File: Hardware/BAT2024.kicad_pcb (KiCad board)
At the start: 2 copper layers, 0 parts

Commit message: Finalized schematic V1.0; minor changes to symbol library
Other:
- board outline added: 80 x 80 mm
- board text added: "Bachelorarbeit 2024 Stefano Nicora HSLU T&A | V1.0"
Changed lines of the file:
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@@
 	)
 	(net 0 "")
+	(gr_circle
+		(center 158.628 97.028)
+		(end 198.628 97.028)
+		(stroke
+			(width 0.2)
+			(type default)
+		)
+		(fill none)
+		(layer "Edge.Cuts")
+	)
+	(gr_text "Bachelorarbeit 2024\nStefano Nicora\nHSLU T&A | V1.0\n"
+		(at 148.336 130.556 0)
+		(layer "F.SilkS")
+		(effects
+			(font
+				(size 1.5 1.5)
+				(thickness 0.3)
+				(bold yes)
+			)
+			(justify left bottom)
+		)
+	)
 )

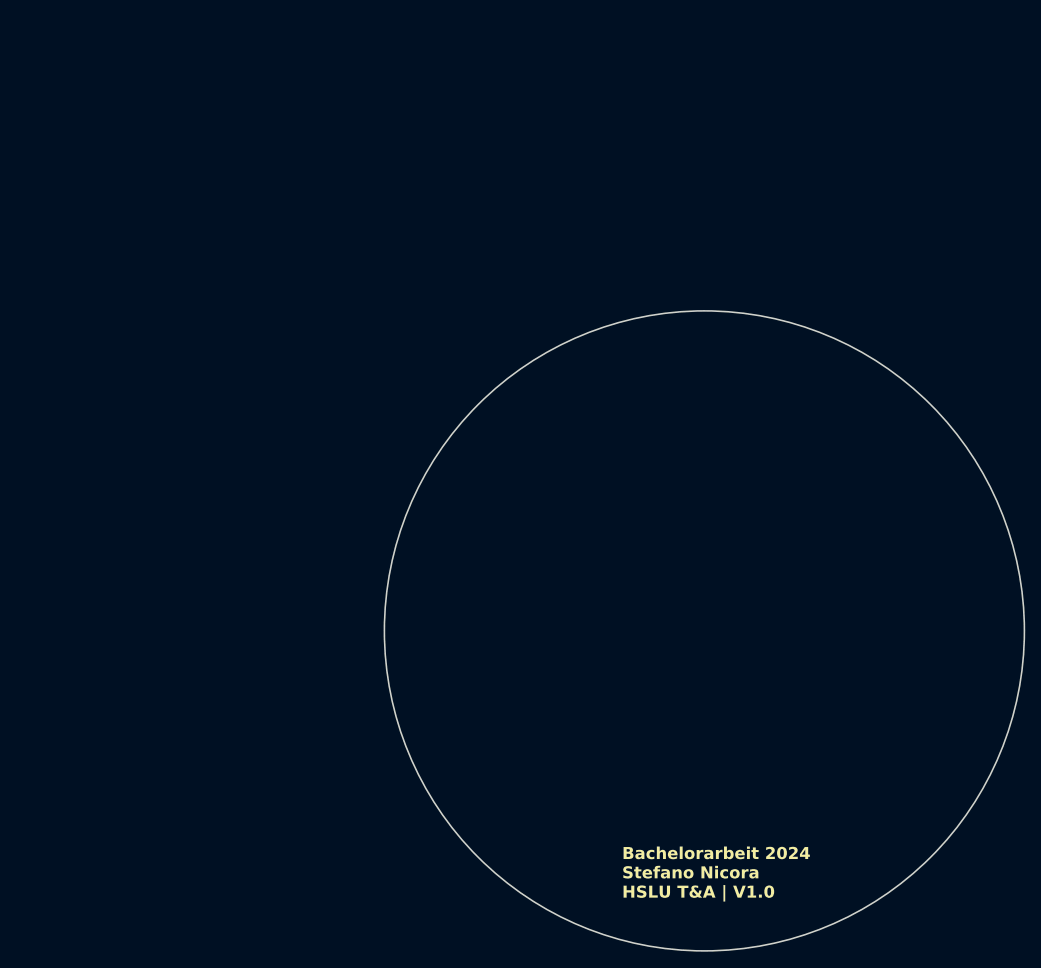
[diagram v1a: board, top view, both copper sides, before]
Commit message: Add temporary layout of footprints on PCB; generate placement-pdf
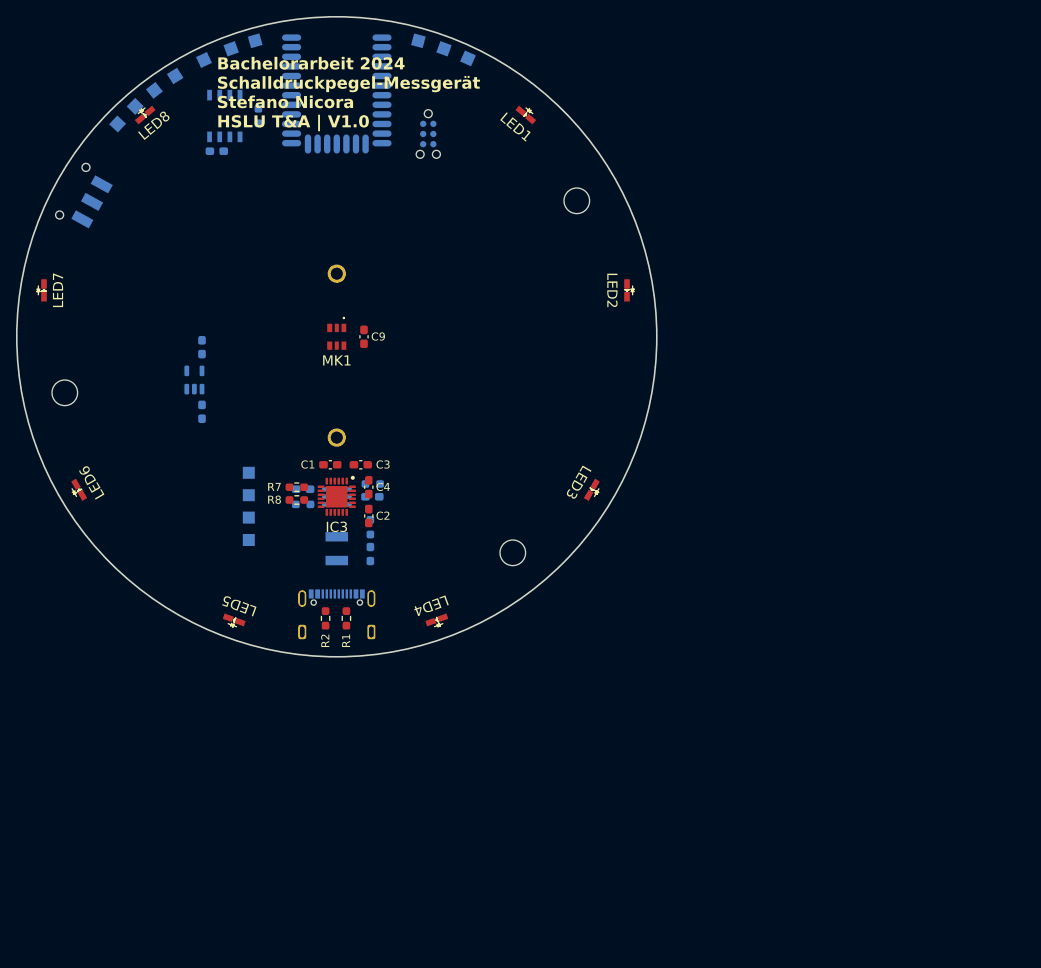
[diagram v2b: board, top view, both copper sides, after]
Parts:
- added C1: 1uF, Capacitor_SMD:C_0603_1608Metric_Pad1.08x0.95mm_HandSolder, F.Cu at (111.9, 76.3)
- added C10: 100nF, Capacitor_SMD:C_0603_1608Metric_Pad1.08x0.95mm_HandSolder, B.Cu at (97.7, 37.1)
- added C2: 1uF, Capacitor_SMD:C_0603_1608Metric_Pad1.08x0.95mm_HandSolder, F.Cu at (116.7, 82.7)
- added C3: 0.47uF, Capacitor_SMD:C_0603_1608Metric_Pad1.08x0.95mm_HandSolder, F.Cu at (115.7, 76.3)
- added C4: 0.47uF, Capacitor_SMD:C_0603_1608Metric_Pad1.08x0.95mm_HandSolder, F.Cu at (116.7, 79.1)
- added C5: 1uF, Capacitor_SMD:C_0603_1608Metric_Pad1.08x0.95mm_HandSolder, B.Cu at (108.5, 79.3)
- added C6: 1uF, Capacitor_SMD:C_0603_1608Metric_Pad1.08x0.95mm_HandSolder, B.Cu at (117.1, 80.3)
- added C7: 1uF, Capacitor_SMD:C_0603_1608Metric_Pad1.08x0.95mm_HandSolder, B.Cu at (95.8, 69.6)
- added C8: 1uF, Capacitor_SMD:C_0603_1608Metric_Pad1.08x0.95mm_HandSolder, B.Cu at (95.8, 61.6)
- added C9: 100nF, Capacitor_SMD:C_0603_1608Metric_Pad1.08x0.95mm_HandSolder, F.Cu at (116.1, 60.3)
- added D1: LED, LED_SMD:LED_0603_1608Metric_Pad1.05x0.95mm_HandSolder, B.Cu at (116.9, 87.4)
- added F1: Littlefuse_1210L020WR, BAT_Footprint-Library:Littlefuse_FUSC3226X100N, B.Cu at (112.7, 86.8)
- added H1: BatteryHolder_1025-7, BAT_Footprint-Library:BatteryHolder_10257, B.Cu at (112.7, 52.4)
- added H2: MountingHole, MountingHole:MountingHole_3.2mm_M3, B.Cu at (142.7, 43.3)
- added H3: MountingHole, MountingHole:MountingHole_3.2mm_M3, B.Cu at (78.7, 67.3)
- added H4: MountingHole, MountingHole:MountingHole_3.2mm_M3, B.Cu at (134.7, 87.3)
- added IC1: BGM220PC22WGA2R, BAT_Footprint-Library:BGM220PC22WGA2R, B.Cu at (112.7, 29.5)
- added IC2: EEPROM_M95P16-IXMNT_E, BAT_Footprint-Library:EEPROM_SOIC127P600X175-8L, B.Cu at (98.7, 32.7)
- added IC3: LED-Driver_LP55231SQX_NOPB, BAT_Footprint-Library:LED-Driver-QFN50P400X400X80-25N, F.Cu at (112.7, 80.3)
- added J1: Conn_ARM_SWD_TagConnect_TC2030-NL, Connector:Tag-Connect_TC2030-IDC-NL_2x03_P1.27mm_Vertical, B.Cu at (124.1, 34.9)
- added J2: USB4105-GF-A-060, BAT_Footprint-Library:GCT_USB4105-GF-A-060, B.Cu at (112.7, 97.2)
- added LED1: LED_XZCM2CRK53WA-8VF, BAT_Footprint-Library:LEDM168X110N, F.Cu at (136.3, 32.5)
- added LED2: LED_XZCM2CRK53WA-8VF, BAT_Footprint-Library:LEDM168X110N, F.Cu at (149.0, 54.5)
- added LED3: LED_XZCM2CRK53WA-8VF, BAT_Footprint-Library:LEDM168X110N, F.Cu at (144.6, 79.4)
- added LED4: LED_XZCM2CRK53WA-8VF, BAT_Footprint-Library:LEDM168X110N, F.Cu at (125.2, 95.7)
- added LED5: LED_XZCM2CRK53WA-8VF, BAT_Footprint-Library:LEDM168X110N, F.Cu at (99.9, 95.7)
- added LED6: LED_XZCM2CRK53WA-8VF, BAT_Footprint-Library:LEDM168X110N, F.Cu at (80.5, 79.4)
- added LED7: LED_XZCM2CRK53WA-8VF, BAT_Footprint-Library:LEDM168X110N, F.Cu at (76.1, 54.5)
- added LED8: LED_XZCM2CRK53WA-8VF, BAT_Footprint-Library:LEDM168X110N, F.Cu at (88.7, 32.5)
- added MK1: MEMS-Microphone_ICS-41351, BAT_Footprint-Library:MEMS-Mikrofon_ICS41351, F.Cu at (112.7, 60.3)
- added R1: 5.1k, Resistor_SMD:R_0603_1608Metric_Pad0.98x0.95mm_HandSolder, F.Cu at (113.9, 95.5)
- added R2: 5.1k, Resistor_SMD:R_0603_1608Metric_Pad0.98x0.95mm_HandSolder, F.Cu at (111.3, 95.5)
- added R3: 10k, Resistor_SMD:R_0603_1608Metric_Pad0.98x0.95mm_HandSolder, B.Cu at (116.9, 84.1)
- added R4: 10k, Resistor_SMD:R_0603_1608Metric_Pad0.98x0.95mm_HandSolder, B.Cu at (117.2, 78.7)
- added R5: 10k, Resistor_SMD:R_0603_1608Metric_Pad0.98x0.95mm_HandSolder, B.Cu at (108.5, 81.2)
- added R6: 10k, Resistor_SMD:R_0603_1608Metric_Pad0.98x0.95mm_HandSolder, B.Cu at (102.9, 32.7)
- added R7: 10k, Resistor_SMD:R_0603_1608Metric_Pad0.98x0.95mm_HandSolder, F.Cu at (107.7, 79.1)
- added R8: 10k, Resistor_SMD:R_0603_1608Metric_Pad0.98x0.95mm_HandSolder, F.Cu at (107.7, 80.7)
- added S1: JS102011SAQN, BAT_Footprint-Library:C-K_Switch_JS102011SAQN, B.Cu at (79.7, 42.1)
- added TP1: VCC, BAT_Footprint-Library:TestPoint_Pad_1.5x1.5mm, B.Cu at (101.7, 85.7)
- added TP10: MOSI, BAT_Footprint-Library:TestPoint_Pad_1.5x1.5mm, B.Cu at (87.5, 31.5)
- added TP11: MISO, BAT_Footprint-Library:TestPoint_Pad_1.5x1.5mm, B.Cu at (85.3, 33.7)
- added TP12: CLK, BAT_Footprint-Library:TestPoint_Pad_1.5x1.5mm, B.Cu at (92.5, 27.7)
- added TP13: PDM_CLK, BAT_Footprint-Library:TestPoint_Pad_1.5x1.5mm, B.Cu at (126.1, 24.3)
- added TP14: PDM_DATA0, BAT_Footprint-Library:TestPoint_Pad_1.5x1.5mm, B.Cu at (122.9, 23.3)
- added TP2: +BATT, BAT_Footprint-Library:TestPoint_Pad_1.5x1.5mm, B.Cu at (101.7, 80.1)
- added TP3: +3V3, BAT_Footprint-Library:TestPoint_Pad_1.5x1.5mm, B.Cu at (101.7, 77.3)
- added TP4: GND, BAT_Footprint-Library:TestPoint_Pad_1.5x1.5mm, B.Cu at (129.1, 25.5)
- added TP5: GND, BAT_Footprint-Library:TestPoint_Pad_1.5x1.5mm, B.Cu at (96.1, 25.7)
- added TP6: GND, BAT_Footprint-Library:TestPoint_Pad_1.5x1.5mm, B.Cu at (101.7, 82.9)
- added TP7: SDA, BAT_Footprint-Library:TestPoint_Pad_1.5x1.5mm, B.Cu at (99.5, 24.3)
- added TP8: SCL, BAT_Footprint-Library:TestPoint_Pad_1.5x1.5mm, B.Cu at (102.5, 23.3)
- added TP9: CS, BAT_Footprint-Library:TestPoint_Pad_1.5x1.5mm, B.Cu at (89.9, 29.5)
- added U1: MIC5504-3.3YM5, Package_TO_SOT_SMD:SOT-23-5, B.Cu at (94.9, 65.7)
- added U2: BQ21040DBVR, BAT_Footprint-Library:BatteryManagement_SOT95P280X145-6N, B.Cu at (112.7, 80.3)
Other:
- board text added: "Bachelorarbeit 2024 Schalldruckpegel-Messgerät Stefano Nicora HSLU T&A | V1.0"
- board text added: "CLK"
- board text added: "GND"
- board text added: "IO"
- board text added: "RST"
- board text added: "SWO"
- board text added: "VCC"
- board text removed: "Bachelorarbeit 2024 Stefano Nicora HSLU T&A | V1.0"

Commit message: Created first layout
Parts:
- moved R8 38.5 mm to (94.0, 44.7), turned to -90 degrees
- moved R7 36.5 mm to (95.6, 44.7), turned to -90 degrees
- moved LED8 36.5 mm to (125.2, 32.7), turned to 155 degrees
- moved LED7 36.2 mm to (104.5, 32.1), turned to -155 degrees
- moved C2 35.9 mm to (93.6, 55.2)
- moved IC3 35.7 mm to (94.4, 49.7), turned to 180 degrees
- moved LED6 34.3 mm to (89.5, 46.3), turned to -120 degrees
- moved C4 32.1 mm to (96.2, 54.3), turned to 180 degrees
- moved LED5 30.6 mm to (89.0, 67.0), turned to -70 degrees
- moved C1 30.4 mm to (98.8, 48.9), turned to 90 degrees
- moved C3 29.0 mm to (98.8, 52.7), turned to -90 degrees
- moved LED4 25.9 mm to (103.2, 82.0), turned to -25 degrees
- moved TP6 22.9 mm to (91.6, 62.3)
- moved LED3 20.9 mm to (123.9, 82.5), turned to 20 degrees
- moved LED2 17.1 mm to (138.9, 68.3), turned to 65 degrees
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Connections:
- net Net-(F1-Pad1) renamed Fuse
- C8 pad 1: +3.3V -> +3.3
- J1 pad 1: VCC -> +3.3V
- J2 pad A7: /RESET -> /SWDIO
- J2 pad B7: /SWDIO -> /RESET
- S1 pad 1: Net-(U1-VOUT) -> +3.3
- TP3 pad 1: +3.3V -> +3.3
- U1 pad 5: Net-(U1-VOUT) -> +3.3
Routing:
- net /LED1: track 0.00 -> 95.4 mm
- net +3.3V: track 0.00 -> 92.0 mm, vias 0 -> 5
- net /LED2: track 0.00 -> 77.1 mm
- net GND: track 0.00 -> 75.2 mm, vias 0 -> 294
- net /RESET: track 0.00 -> 66.2 mm, vias 0 -> 3
- net /LED3: track 0.00 -> 58.3 mm
- net /SWCLK: track 0.00 -> 56.7 mm, vias 0 -> 2
- net /SWDIO: track 0.00 -> 54.3 mm, vias 0 -> 4
- net /SWO: track 0.00 -> 51.8 mm, vias 0 -> 2
- net /LED8: track 0.00 -> 42.8 mm
- net /LED4: track 0.00 -> 39.2 mm
- net /I2C_SDA: track 0.00 -> 35.1 mm, vias 0 -> 3
- net +BATT: track 0.00 -> 34.8 mm, vias 0 -> 2
- net /I2C_SCL: track 0.00 -> 34.7 mm, vias 0 -> 3
- net /PDM_CLK: track 0.00 -> 34.0 mm, vias 0 -> 1
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- added copper zone on B.Cu, net GND
- added copper zone on F.Cu, net GND
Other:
- board size 80 x 80 mm -> 60 x 60 mm
- board text added: "CS"
- board text added: "DATA0"
- board text added: "MISO"
- board text added: "MOSI"
- board text added: "SCK"
- board text added: "SCL"
- board text added: "SDA"
